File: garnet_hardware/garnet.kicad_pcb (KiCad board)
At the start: 4 copper layers, 165 x 50 mm, 82 parts, among them Q3 G50N03K, Q4 G50N03K, Q5 G50N03K, Q6 G50N03K, U1 ESP32-S3-MINI-1U, U2 TPS561208, U3 MCP33141D-10, U4 OPA1664PW, U5 TLV761, U6 MCP33141D-10, U7 L6385E, U8 L6385E

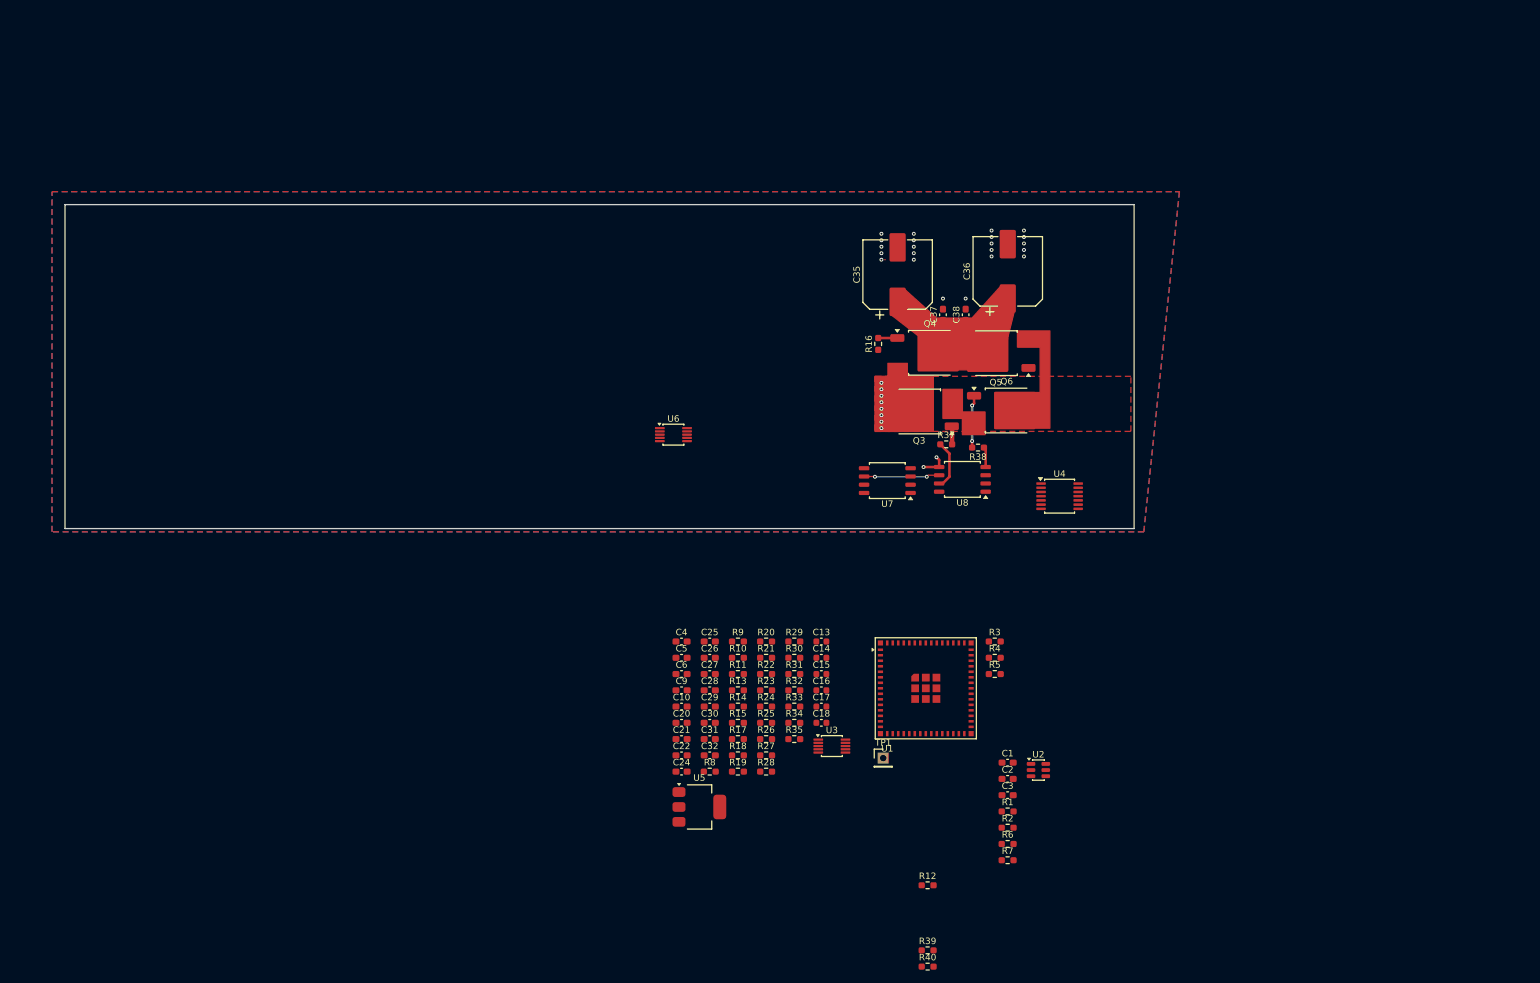
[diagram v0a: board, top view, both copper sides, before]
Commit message: power frount end and sd card layed out on PCB
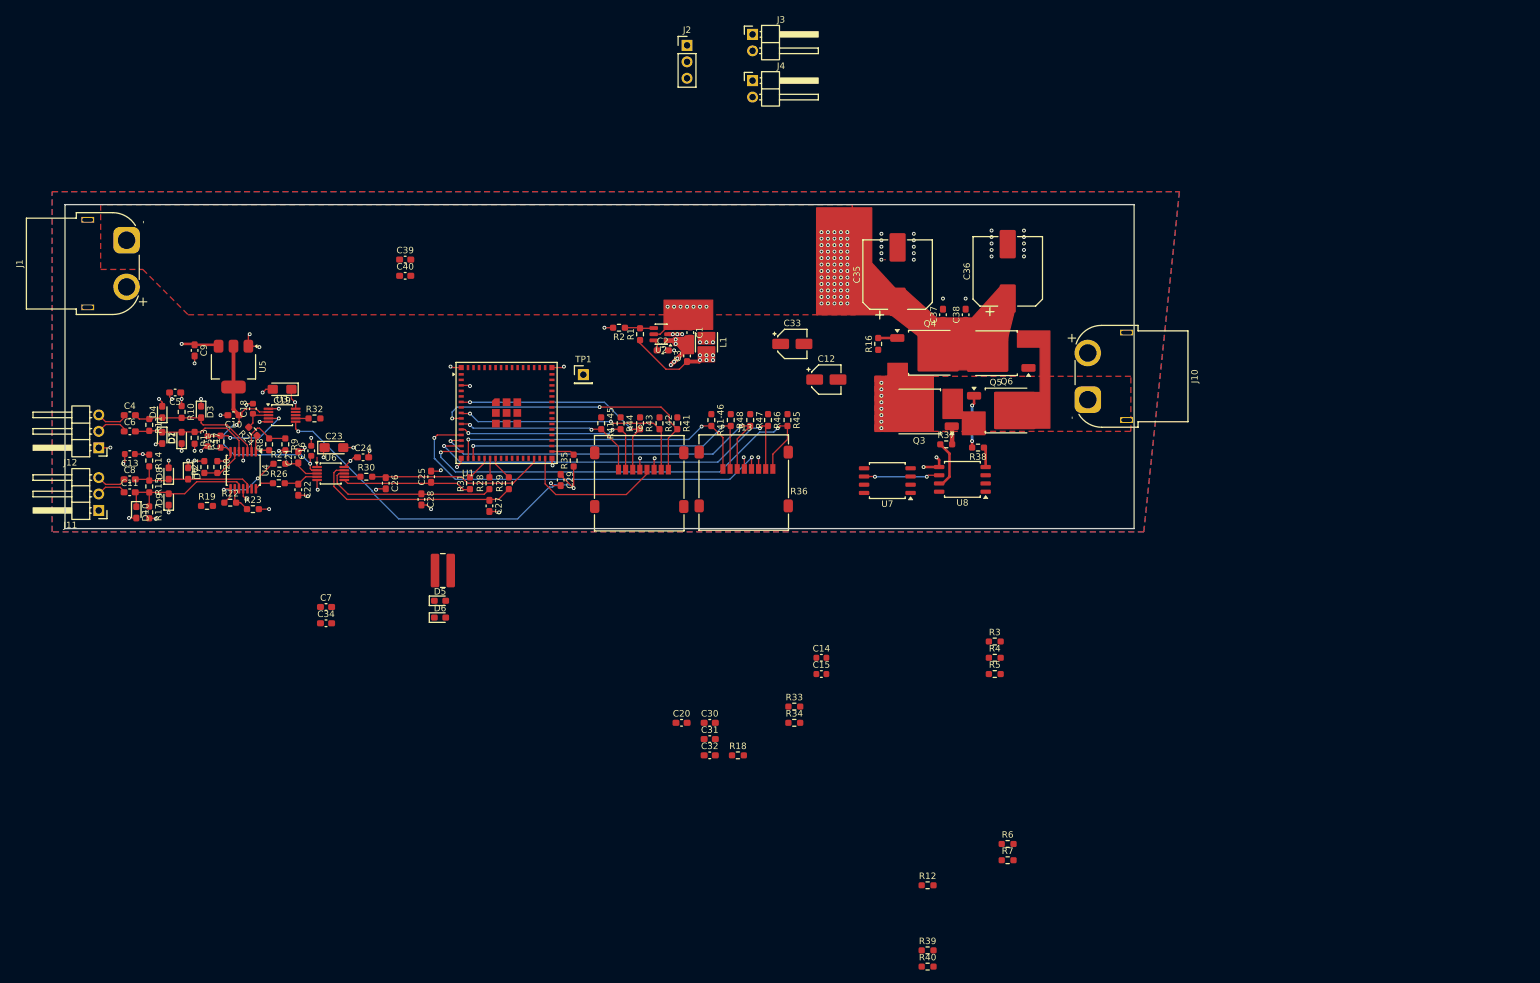
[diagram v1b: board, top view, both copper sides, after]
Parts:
- added C11: TBD, Capacitor_SMD:C_0603_1608Metric_Pad1.08x0.95mm_HandSolder, F.Cu at (46.0, 97.4)
- added C12: 10u, Capacitor_SMD:CP_Elec_4x4.5, F.Cu at (153.5, 80.0)
- added C19: 10uF, Capacitor_Tantalum_SMD:CP_EIA-3216-10_Kemet-I_HandSolder, F.Cu at (69.5, 81.5)
- added C23: 10uF, Capacitor_Tantalum_SMD:CP_EIA-3216-10_Kemet-I_HandSolder, F.Cu at (77.5, 90.5)
- added C33: 10uF, Capacitor_SMD:CP_Elec_4x4.5, F.Cu at (148.2, 74.5)
- added C34: 1u, Capacitor_SMD:C_0603_1608Metric_Pad1.08x0.95mm_HandSolder, F.Cu at (76.3, 117.6)
- added C39: 1uF, Capacitor_SMD:C_0603_1608Metric_Pad1.08x0.95mm_HandSolder, F.Cu at (88.5, 61.5)
- added C40: 1uF, Capacitor_SMD:C_0603_1608Metric_Pad1.08x0.95mm_HandSolder, F.Cu at (88.5, 64.0)
- added C7: 1u, Capacitor_SMD:C_0603_1608Metric_Pad1.08x0.95mm_HandSolder, F.Cu at (76.3, 115.1)
- added C8: TBD, Capacitor_SMD:C_0603_1608Metric_Pad1.08x0.95mm_HandSolder, F.Cu at (46.0, 95.4)
- added D1: D, Diode_SMD:D_0603_1608Metric_Pad1.05x0.95mm_HandSolder, F.Cu at (54.0, 89.0)
- added D10: D, Diode_SMD:D_0603_1608Metric_Pad1.05x0.95mm_HandSolder, F.Cu at (47.0, 100.5)
- added D2: D, Diode_SMD:D_0603_1608Metric_Pad1.05x0.95mm_HandSolder, F.Cu at (51.0, 89.0)
- added D3: D, Diode_SMD:D_0603_1608Metric_Pad1.05x0.95mm_HandSolder, F.Cu at (57.0, 85.0)
- added D4: D, Diode_SMD:D_0603_1608Metric_Pad1.05x0.95mm_HandSolder, F.Cu at (51.0, 85.0)
- added D5: D, Diode_SMD:D_0603_1608Metric_Pad1.05x0.95mm_HandSolder, F.Cu at (93.9, 114.1)
- added D6: D, Diode_SMD:D_0603_1608Metric_Pad1.05x0.95mm_HandSolder, F.Cu at (93.9, 116.7)
- added D7: D, Diode_SMD:D_0603_1608Metric_Pad1.05x0.95mm_HandSolder, F.Cu at (55.0, 94.5)
- added D8: D, Diode_SMD:D_0603_1608Metric_Pad1.05x0.95mm_HandSolder, F.Cu at (52.0, 94.5)
- added D9: D, Diode_SMD:D_0603_1608Metric_Pad1.05x0.95mm_HandSolder, F.Cu at (52.0, 98.5)
- added J1: BATT, Connector_AMASS:AMASS_XT60PW-F_1x02_P7.20mm_Horizontal, F.Cu at (45.5, 58.5)
- added J10: Conn_01x02_Pin, Connector_AMASS:AMASS_XT60PW-F_1x02_P7.20mm_Horizontal, F.Cu at (193.8, 83.1)
- added J11: PZ2, Connector_PinHeader_2.54mm:PinHeader_1x03_P2.54mm_Horizontal, F.Cu at (41.2, 100.2)
- added J12: PZ1, Connector_PinHeader_2.54mm:PinHeader_1x03_P2.54mm_Horizontal, F.Cu at (41.2, 90.5)
- added J13: SD_A, Connector_Card:microSD_HC_Molex_47219-2001, F.Cu at (140.8, 95.9)
- added J2: USB, Connector_PinHeader_2.54mm:PinHeader_1x03_P2.54mm_Vertical, F.Cu at (132.0, 28.4)
- added J3: actuator PTC, Connector_PinHeader_2.54mm:PinHeader_1x02_P2.54mm_Horizontal, F.Cu at (142.1, 26.7)
- added J4: batt PTC, Connector_PinHeader_2.54mm:PinHeader_1x02_P2.54mm_Horizontal, F.Cu at (142.1, 33.9)
- added J9: SD_A, Connector_Card:microSD_HC_Molex_47219-2001, F.Cu at (124.6, 96.0)
- added L1: 3.3uH, Inductor_SMD:L_Neosid_SMS-ME3010, F.Cu at (135.0, 74.2)
- added R36: R, Resistor_SMD:R_1020_2550Metric_Pad1.33x5.20mm_HandSolder, F.Cu at (94.3, 109.5)
- added R41: 10K, Resistor_SMD:R_0603_1608Metric_Pad0.98x0.95mm_HandSolder, F.Cu at (130.5, 86.8)
- added R41-45: 10K, Resistor_SMD:R_0603_1608Metric_Pad0.98x0.95mm_HandSolder, F.Cu at (118.8, 86.8)
- added R41-46: 10K, Resistor_SMD:R_0603_1608Metric_Pad0.98x0.95mm_HandSolder, F.Cu at (135.8, 86.2)
- added R42: 10K, Resistor_SMD:R_0603_1608Metric_Pad0.98x0.95mm_HandSolder, F.Cu at (127.8, 86.8)
- added R43: 10K, Resistor_SMD:R_0603_1608Metric_Pad0.98x0.95mm_HandSolder, F.Cu at (124.8, 86.8)
- added R44: 10K, Resistor_SMD:R_0603_1608Metric_Pad0.98x0.95mm_HandSolder, F.Cu at (121.8, 86.8)
- added R45: 10K, Resistor_SMD:R_0603_1608Metric_Pad0.98x0.95mm_HandSolder, F.Cu at (147.5, 86.2)
- added R46: 10K, Resistor_SMD:R_0603_1608Metric_Pad0.98x0.95mm_HandSolder, F.Cu at (144.5, 86.2)
- added R47: 10K, Resistor_SMD:R_0603_1608Metric_Pad0.98x0.95mm_HandSolder, F.Cu at (141.8, 86.2)
- added R48: 10K, Resistor_SMD:R_0603_1608Metric_Pad0.98x0.95mm_HandSolder, F.Cu at (138.8, 86.2)
- R39, R40: value R -> 5R
- moved U4 126.1 mm to (63.5, 94.0), turned to -90 degrees
- moved C13 110.6 mm to (46.0, 91.5), turned to 180 degrees
- moved C17 103.2 mm to (58.0, 89.5), turned to -90 degrees
- moved C18 100.2 mm to (65.0, 84.5), turned to 90 degrees
- moved U3 99.0 mm to (69.5, 85.5)
- moved U5 98.9 mm to (62.0, 78.0), turned to -90 degrees
- moved R11 98.7 mm to (49.0, 87.0), turned to -90 degrees
- moved R14 98.5 mm to (49.0, 92.5), turned to -90 degrees
- moved R15 97.9 mm to (49.0, 96.5), turned to -90 degrees
- moved R2 97.7 mm to (121.5, 72.0), turned to 180 degrees
- moved R17 97.4 mm to (49.0, 100.5), turned to -90 degrees
- moved R25 94.7 mm to (60.0, 89.6), turned to 90 degrees
- moved R10 93.9 mm to (54.0, 85.0), turned to -90 degrees
- moved C6 93.0 mm to (46.0, 88.0)
- moved R1 93.0 mm to (124.8, 73.0), turned to 90 degrees
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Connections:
- C26 pad 1: /pezio sense/SDO1 -> SDO1
- C30 pad 1: /pezio sense/SDO1 -> SDO0
- C35 pad 1: Net-(Q4-D) -> VBUS
- C36 pad 1: Net-(Q4-D) -> VBUS
- C37 pad 1: Net-(Q4-D) -> VBUS
- C38 pad 1: Net-(Q4-D) -> VBUS
- Q4 pad 2: Net-(Q4-D) -> VBUS
- Q5 pad 2: Net-(Q4-D) -> VBUS
- R14 pad 2: Net-(U4C-+) -> Net-(D7-A)
- R15 pad 1: Net-(U4C-+) -> Net-(D7-A)
- R15 pad 2: Net-(U4D-+) -> Net-(D10-K)
- R17 pad 1: Net-(U4D-+) -> Net-(D10-K)
- R18 pad 2: Net-(U4C--) -> Net-(U4D--)
- R19 pad 1: Net-(U4C--) -> Net-(U4D--)
- R22 pad 2: Net-(U4D--) -> Net-(U4C--)
- R23 pad 1: Net-(U4D--) -> Net-(U4C--)
- R28 pad 2: /pezio sense/SCLK1 -> SCLK1
- R29 pad 2: /pezio sense/SDI1 -> SDI1
- R30 pad 2: /pezio sense/SDO1 -> SDO1
- R31 pad 2: /pezio sense/CNVST1 -> CNVST1
- R32 pad 2: /pezio sense/SDO1 -> SDO0
- R33 pad 2: /pezio sense/SCLK1 -> SCLK0
- R34 pad 2: /pezio sense/SDI1 -> SDI0
- R35 pad 2: /pezio sense/CNVST1 -> CNVST0
- R6 pad 2: /BMS/Vsense -> Vsense
- R7 pad 1: /BMS/Vsense -> Vsense
- U1 pad 10: unconnected-(U1-IO6-Pad10) -> DAT2_A
- U1 pad 11: unconnected-(U1-IO7-Pad11) -> DAT3_A
- U1 pad 12: unconnected-(U1-IO8-Pad12) -> CLK_B
- U1 pad 13: unconnected-(U1-IO9-Pad13) -> CMD_B
- U1 pad 14: unconnected-(U1-IO10-Pad14) -> DAT0_B
- U1 pad 15: unconnected-(U1-IO11-Pad15) -> DAT1_B
- U1 pad 16: unconnected-(U1-IO12-Pad16) -> DAT2_B
- U1 pad 17: unconnected-(U1-IO13-Pad17) -> DAT3_B
- U1 pad 18: unconnected-(U1-IO14-Pad18) -> actuator PTC
- U1 pad 19: unconnected-(U1-IO15-Pad19) -> CNVST1
- U1 pad 20: unconnected-(U1-IO16-Pad20) -> SCLK1
- U1 pad 21: unconnected-(U1-IO17-Pad21) -> SDI1
- U1 pad 22: unconnected-(U1-IO18-Pad22) -> SCLK0
- U1 pad 25: unconnected-(U1-IO21-Pad25) -> SDI0
- U1 pad 27: unconnected-(U1-IO47-Pad27) -> /actuator drive/LINB
- U1 pad 28: unconnected-(U1-IO33-Pad28) -> SDO1
- U1 pad 29: unconnected-(U1-IO34-Pad29) -> SDO0
- U1 pad 30: unconnected-(U1-IO48-Pad30) -> CLK_A
- U1 pad 31: unconnected-(U1-IO35-Pad31) -> CNVST0
- U1 pad 38: unconnected-(U1-IO42-Pad38) -> /actuator drive/HINA
- U1 pad 4: batt PTC -> unconnected-(U1-IO0-Pad4)
- U1 pad 41: unconnected-(U1-IO45-Pad41) -> /actuator drive/HINB
- U1 pad 44: unconnected-(U1-IO46-Pad44) -> /actuator drive/LINA
- U1 pad 5: actuator PTC -> Vsense
- U1 pad 6: unconnected-(U1-IO2-Pad6) -> CMD_A
- U1 pad 7: unconnected-(U1-IO3-Pad7) -> batt PTC
- U1 pad 8: unconnected-(U1-IO4-Pad8) -> DAT0_A
- U1 pad 9: unconnected-(U1-IO5-Pad9) -> DAT1_A
- U4 pad 10: Net-(U4C-+) -> Net-(D10-K)
- U4 pad 12: Net-(U4D-+) -> Net-(D7-A)
- U4 pad 14: /pezio sense/PZ_2_AMP1_N -> /pezio sense/PZ_2_AMP1_P
- U4 pad 8: /pezio sense/PZ_2_AMP1_P -> /pezio sense/PZ_2_AMP1_N
- U6 pad 3: /pezio sense/PZ_2_AMP2_P -> /pezio sense/PZ_2_AMP2_N
- U6 pad 4: /pezio sense/PZ_2_AMP2_N -> /pezio sense/PZ_2_AMP2_P
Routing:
- net DAT1_B: track 0.00 -> 68.9 mm, vias 0 -> 2
- net DAT0_B: track 0.00 -> 62.9 mm, vias 0 -> 2
- net GND: track 0.10 -> 61.4 mm, vias 22 -> 66
- net CLK_B: track 0.00 -> 61.2 mm, vias 0 -> 2
- net Net-(U3-CNVST): track 0.00 -> 58.6 mm, vias 0 -> 2
- net CMD_B: track 0.00 -> 58.2 mm, vias 0 -> 2
- net DAT3_B: track 0.00 -> 49.6 mm, vias 0 -> 2
- net DAT2_B: track 0.00 -> 48.7 mm, vias 0 -> 2
- net DAT1_A: track 0.00 -> 46.2 mm, vias 0 -> 2
- net +3V3: track 0.00 -> 45.0 mm, vias 0 -> 21
- net +1V8: track 0.00 -> 39.7 mm, vias 0 -> 2
- net DAT0_A: track 0.00 -> 38.0 mm, vias 0 -> 2
- net CMD_A: track 0.00 -> 36.1 mm, vias 0 -> 2
- net Net-(U6-SDI): track 0.00 -> 32.4 mm
- net DAT3_A: track 0.00 -> 31.7 mm, vias 0 -> 2
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- added copper zone on In1.Cu, net +3V3
- added copper zone on F.Cu, net VBUS
- added copper zone on In2.Cu, net VBUS

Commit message: cleaned SPI lines, replaced MOSFETS with more sutible ones, added free wheeling diodes added current sensing
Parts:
- removed J13: SD_A, Connector_Card:microSD_HC_Molex_47219-2001
- removed Q3, Q4: G50N03K, Package_TO_SOT_SMD:TO-252-2
- removed R41-46, R47, R48: 10K, Resistor_SMD:R_0603_1608Metric_Pad0.98x0.95mm_HandSolder
- added C41: 1uF, Capacitor_SMD:C_0603_1608Metric_Pad1.08x0.95mm_HandSolder, F.Cu at (252.9, 41.8)
- added C42: 1uF, Capacitor_SMD:C_0603_1608Metric_Pad1.08x0.95mm_HandSolder, F.Cu at (252.9, 44.3)
- added C43: 2.2nF, Capacitor_SMD:C_0603_1608Metric_Pad1.08x0.95mm_HandSolder, F.Cu at (252.9, 46.8)
- added C44: TBD, Capacitor_SMD:C_0603_1608Metric_Pad1.08x0.95mm_HandSolder, F.Cu at (252.9, 49.3)
- added D11: MBRB4030, Package_TO_SOT_SMD:TO-263-2, F.Cu at (243.7, 46.7)
- added D12: MBRB4030, Package_TO_SOT_SMD:TO-263-2, F.Cu at (243.7, 59.0)
- added D13: MBRB4030, Package_TO_SOT_SMD:TO-263-2, F.Cu at (243.7, 71.4)
- added D14: MBRB4030, Package_TO_SOT_SMD:TO-263-2, F.Cu at (243.7, 83.7)
- added Q7: G025N03T, Package_TO_SOT_THT:TO-220-3_Vertical, F.Cu at (253.9, 57.0)
- added Q8: G025N03T, Package_TO_SOT_THT:TO-220-3_Vertical, F.Cu at (253.9, 62.9)
- added R49: 33R, Resistor_SMD:R_0603_1608Metric_Pad0.98x0.95mm_HandSolder, F.Cu at (252.9, 51.8)
- added RN1: 10K, Resistor_SMD:R_Array_Convex_2x0606, F.Cu at (257.7, 71.1)
- added U10: LM321, Package_TO_SOT_SMD:SOT-23-5, F.Cu at (253.3, 72.0)
- added U9: MCP33141D-025-E/MS, Package_SO:MSOP-10_3x3mm_P0.5mm, F.Cu at (254.3, 67.3)
- Q5, Q6: value G50N03K -> G025N03T; footprint Package_TO_SOT_SMD:TO-252-2 -> Package_TO_SOT_THT:TO-220-3_Vertical
- R36: value R -> 1m; footprint Resistor_SMD:R_1020_2550Metric_Pad1.33x5.20mm_HandSolder -> Resistor_SMD:R_2512_6332Metric_Pad1.40x3.35mm_HandSolder
- R46: value 10K -> 15R
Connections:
- C25 pad 1: Net-(U6-CNVST) -> /pezio sense/SDI1
- C27 pad 1: Net-(U6-SDI) -> /pezio sense/SCLK1
- C28 pad 1: Net-(U6-SCLK) -> /pezio sense/CNVST1
- C29 pad 1: Net-(U3-CNVST) -> /pezio sense/SDI0
- C31 pad 1: Net-(U3-SDI) -> /pezio sense/SCLK0
- C32 pad 1: Net-(U3-SCLK) -> /pezio sense/CNVST0
- C40 pad 1: +3V3 -> GND
- C40 pad 2: GND -> +3V3
- J10 pad 1: Net-(J10-Pin_1) -> Net-(D13-A)
- Q5 pad 3: Net-(Q5-S) -> Net-(D11-A)
- Q6 pad 2: Net-(Q5-S) -> VBUS
- Q6 pad 3: Net-(Q3-S) -> Net-(D13-A)
- R16 pad 2: Net-(Q4-G) -> Net-(Q6-G)
- R28 pad 1: Net-(U6-SCLK) -> /pezio sense/CNVST1
- R28 pad 2: SCLK1 -> CNVST1
- R29 pad 1: Net-(U6-SDI) -> /pezio sense/SCLK1
- R29 pad 2: SDI1 -> SCLK1
- R31 pad 1: Net-(U6-CNVST) -> /pezio sense/SDI1
- R31 pad 2: CNVST1 -> SDI1
- R33 pad 1: Net-(U3-SCLK) -> /pezio sense/CNVST0
- R33 pad 2: SCLK0 -> CNVST0
- R34 pad 1: Net-(U3-SDI) -> /pezio sense/SCLK0
- R34 pad 2: SDI0 -> SCLK0
- R35 pad 1: Net-(U3-CNVST) -> /pezio sense/SDI0
- R35 pad 2: CNVST0 -> SDI0
- R36 pad 1: Net-(Q3-S) -> Net-(D12-A)
- R38 pad 2: Net-(Q6-G) -> Net-(Q7-G)
- R45 pad 1: +3V3 -> Href
- R45 pad 2: DAT1_B -> GND
- R46 pad 1: +3V3 -> Net-(U11-IN+)
- R46 pad 2: DAT0_B -> Net-(R46-Pad2)
- U1 pad 12: CLK_B -> unconnected-(U1-IO8-Pad12)
- U1 pad 13: CMD_B -> unconnected-(U1-IO9-Pad13)
- U1 pad 14: DAT0_B -> unconnected-(U1-IO10-Pad14)
- U1 pad 15: DAT1_B -> unconnected-(U1-IO11-Pad15)
- U1 pad 16: DAT2_B -> unconnected-(U1-IO12-Pad16)
- U1 pad 17: DAT3_B -> unconnected-(U1-IO13-Pad17)
- U3 pad 6: Net-(U3-CNVST) -> /pezio sense/CNVST0
- U3 pad 8: Net-(U3-SCLK) -> /pezio sense/SCLK0
- U3 pad 9: Net-(U3-SDI) -> /pezio sense/SDI0
- U6 pad 6: Net-(U6-CNVST) -> /pezio sense/CNVST1
- U6 pad 8: Net-(U6-SCLK) -> /pezio sense/SCLK1
- U6 pad 9: Net-(U6-SDI) -> /pezio sense/SDI1
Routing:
- net (no net): track 0.00 -> 269.7 mm, vias 0 -> 12
- net DAT1_B: track 68.9 -> 0.00 mm, vias 2 -> 0
- net DAT0_B: track 62.9 -> 0.00 mm, vias 2 -> 0
- net unconnected-(U1-IO8-Pad12): track 0.00 -> 61.2 mm, vias 0 -> 2
- net CLK_B: track 61.2 -> 0.00 mm, vias 2 -> 0
- net Net-(U3-CNVST): track 58.6 -> 0.00 mm, vias 2 -> 0
- net unconnected-(U1-IO9-Pad13): track 0.00 -> 58.2 mm, vias 0 -> 2
- net CMD_B: track 58.2 -> 0.00 mm, vias 2 -> 0
- net unconnected-(U1-IO13-Pad17): track 0.00 -> 49.6 mm, vias 0 -> 2
- net DAT3_B: track 49.6 -> 0.00 mm, vias 2 -> 0
- net unconnected-(U1-IO12-Pad16): track 0.00 -> 48.7 mm, vias 0 -> 2
- net DAT2_B: track 48.7 -> 0.00 mm, vias 2 -> 0
- net Net-(U6-SDI): track 32.4 -> 0.00 mm
- net Net-(U6-SCLK): track 27.0 -> 0.00 mm
- net Net-(U6-CNVST): track 20.1 -> 0.00 mm
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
